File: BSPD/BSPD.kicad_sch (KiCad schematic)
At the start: 28 parts, among them J1 350826-1, J2 440054-2, Q1 NMOS, Q2 NMOS, Q3 PMOS, U1 LM339DR, U2 R-78E5.0-0.5, U4 SN74LVC3G14DCUR, U5 NE555DR, U6 SN74LVC1G08DBVR, U7 SN74AC32DR

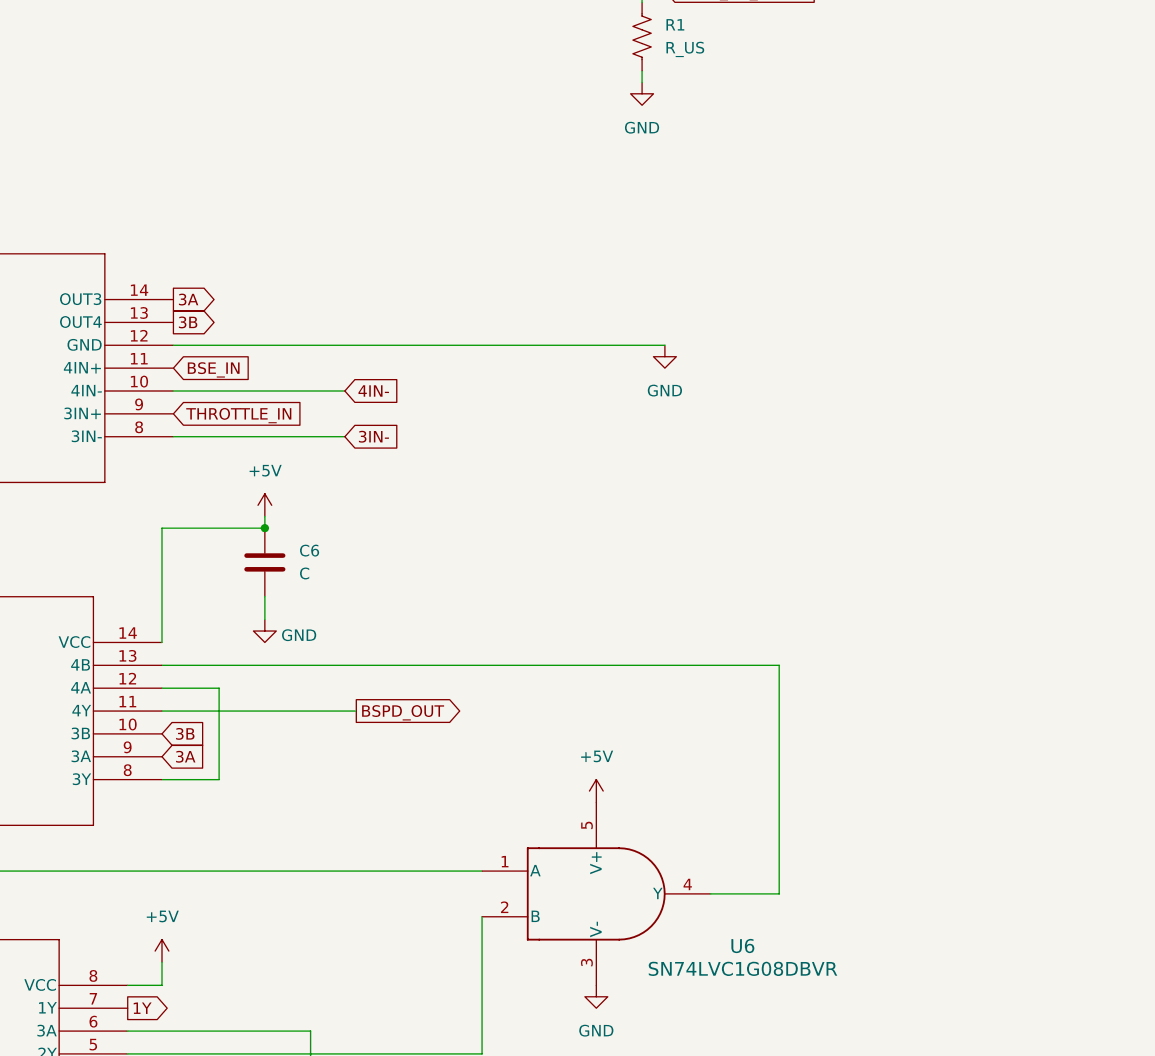
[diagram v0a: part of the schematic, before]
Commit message: Fixed one logical error. Added LT Spice simulation. Pullup Caps, resistor values, schematic layout and cleanup needed.
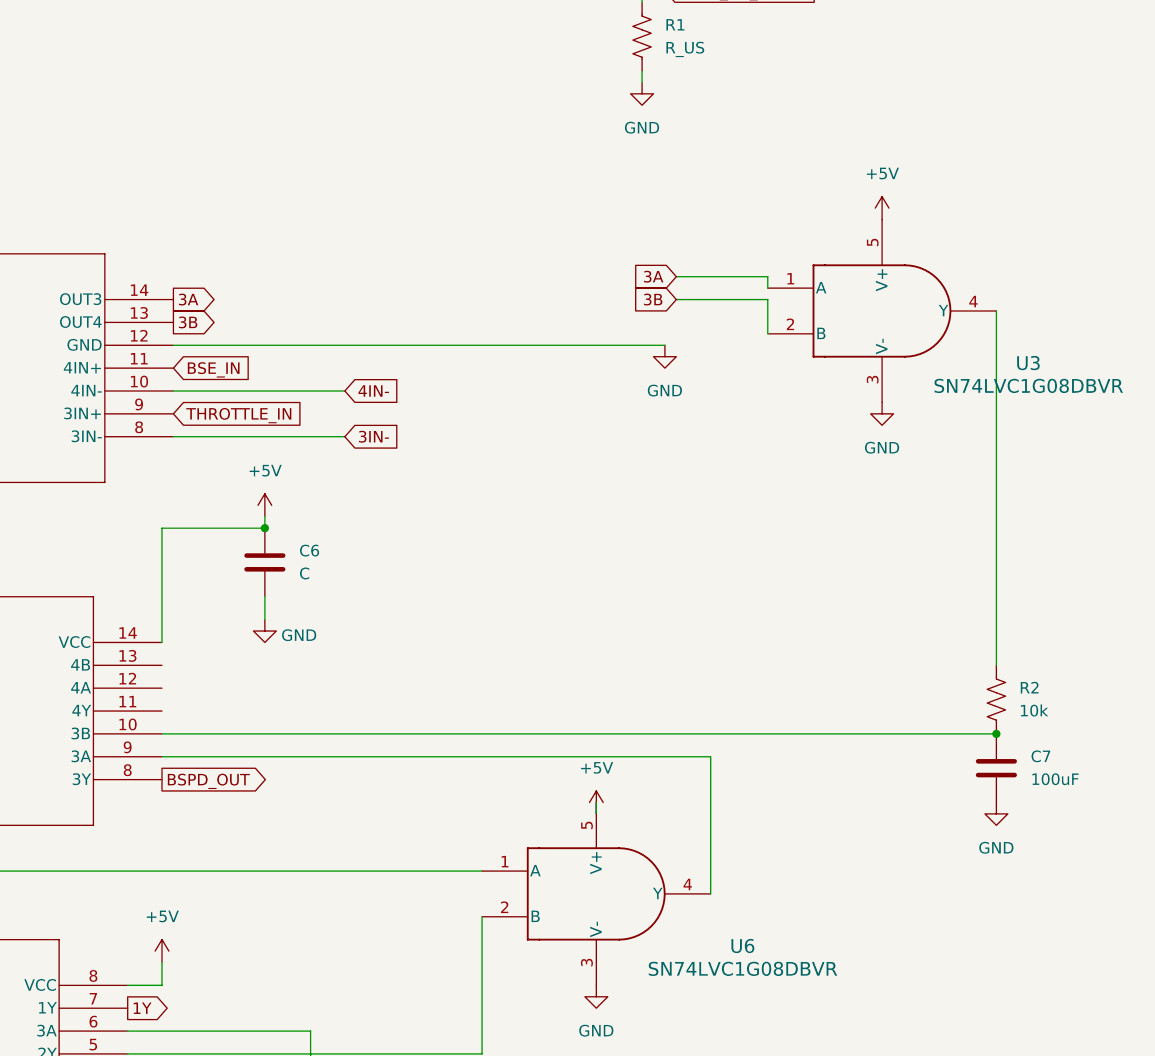
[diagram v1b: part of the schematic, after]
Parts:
- added C7: 100uF, symbol Device:C
- added R2: 10k, symbol Device:R_US
- added U3: SN74LVC1G08DBVR, SN74LVC1G08DBVR:DBV0005A_N, symbol SN74LVC1G08DBVR:SN74LVC1G08DBVR
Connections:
- net 3A: now also U3.1 (A); no longer U7.9 (3A)
- net 3B: now also U3.2 (B); no longer U7.10 (3B)
- net BSPD_OUT: now also U7.8 (3Y); no longer U7.11 (4Y)
- net GND: now also C7.2, U3.3 (V-)
- net at U7.12 (4A): no longer U7.8 (3Y)
- net at U7.13 (4B): no longer U6.4 (Y)
- new net: R2.1, U3.4 (Y)
- new net: C7.1, R2.2, U7.10 (3B)
- new net: U6.4 (Y), U7.9 (3A)

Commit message: Comments on BSPD, TSSI
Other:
- note added: "-AT FAULT - OUTPUT 0V"
- note added: "DC-DC Converter ; 12V-5V ; 500mA"
- note removed: "DC-DC Converter ; 12V-5V"
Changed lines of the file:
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@@
+		)
+	)
+	(text_box "-PLACE VALUES FOR COMPONENETS\n-USE SIMULATION AND VERIFY\n"
+		(exclude_from_sim no)
+		(at 33.02 193.675 0)
+		(size 89.535 13.97)
+		(stroke
+			(width 0)
+			(type default)
+		)
+		(fill
+			(type none)
+		)
+		(effects
+			(font
+				(size 1.27 1.27)
+			)
+			(justify left top)
 		)
 	)
@@
 		(exclude_from_sim no)
 		(at 75.692 176.784 0)
+		(effects
+			(font
+				(size 1.27 1.27)
+			)
+		)
+	)
+	(text "-AT FAULT - OUTPUT 0V\n"
+		(exclude_from_sim no)
+		(at 336.296 62.738 0)
 		(effects
 			(font
@@
 		)
 	)
-	(text "DC-DC Converter ; 12V-5V\n"
+	(text "DC-DC Converter ; 12V-5V ; 500mA\n"
 		(exclude_from_sim no)
-		(at 181.864 46.228 0)
+		(at 186.69 46.736 0)
 		(effects
 			(font

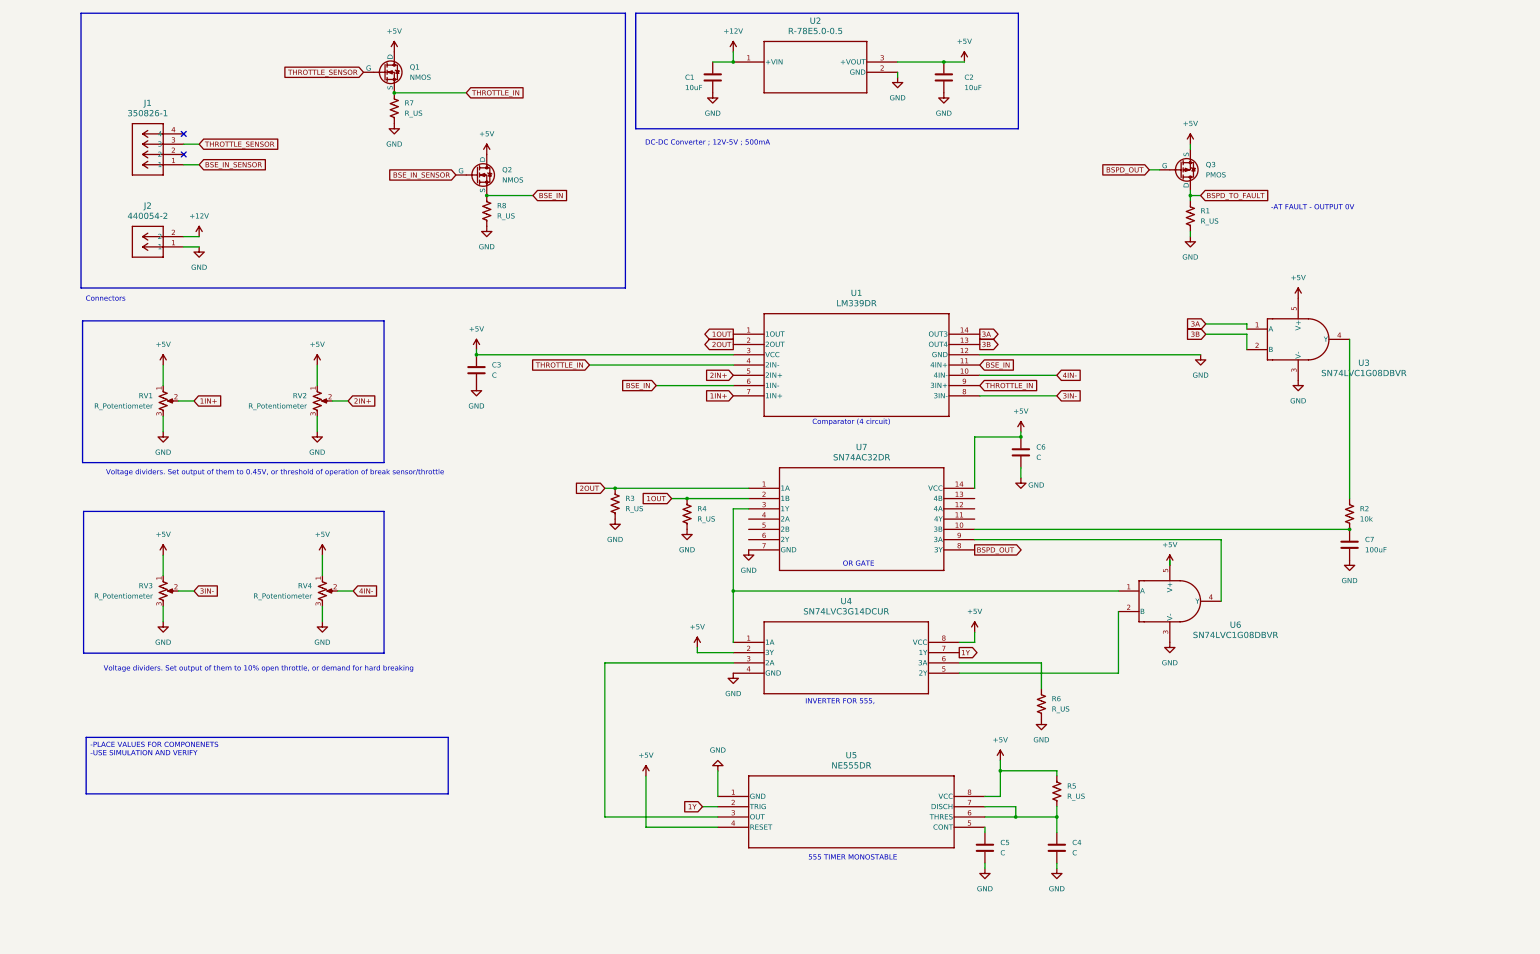
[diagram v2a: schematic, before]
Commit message: Added theory of operation to BSPD
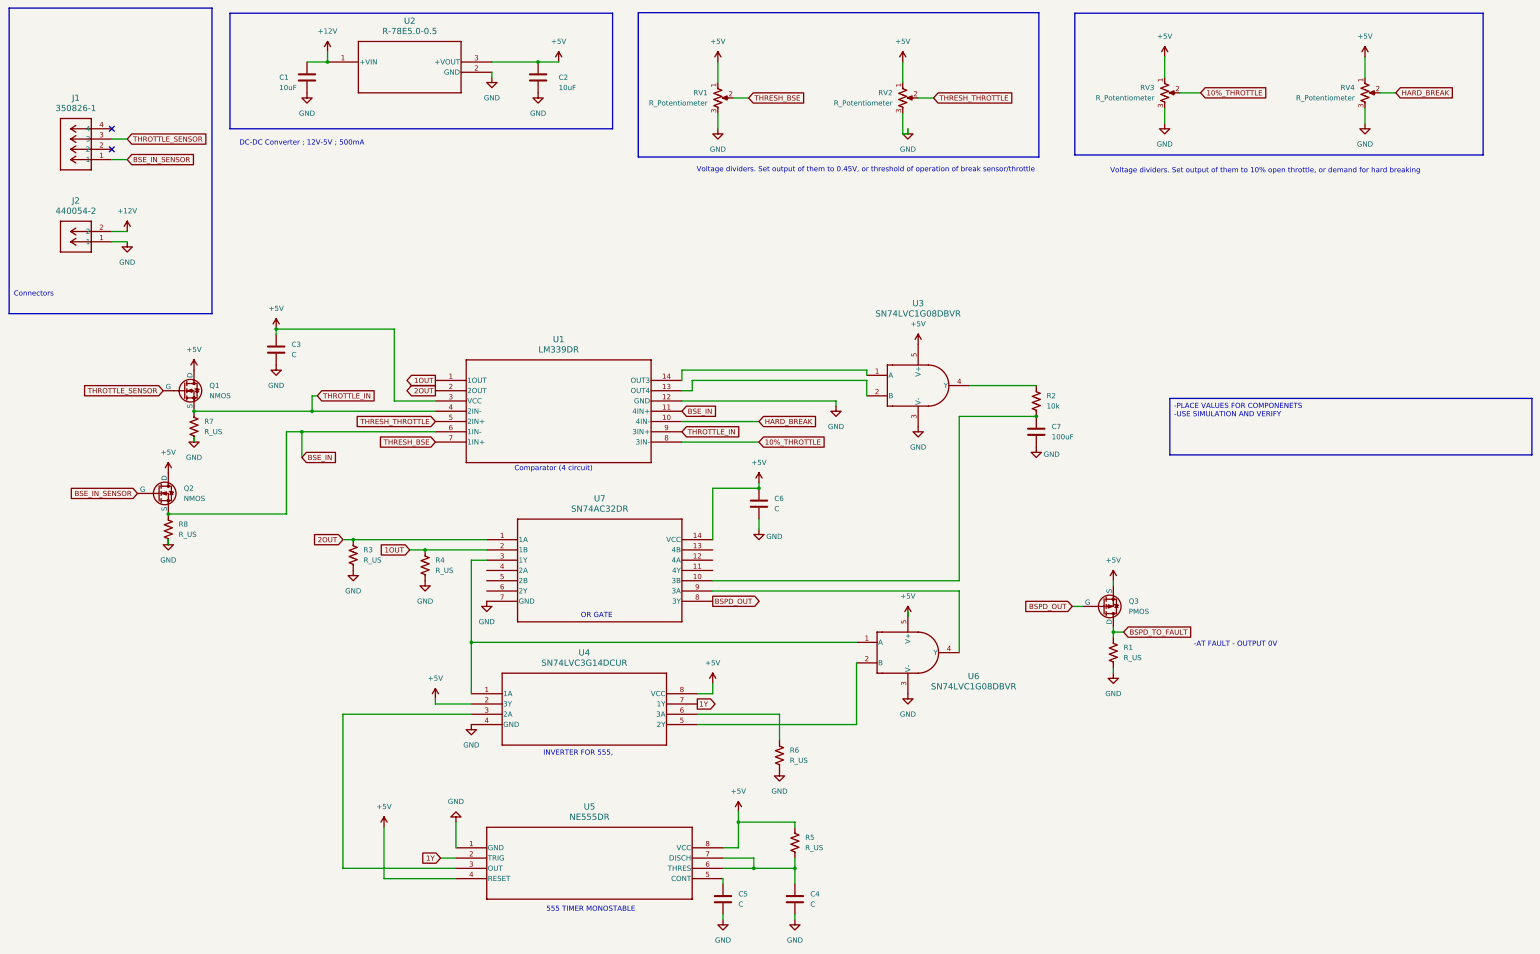
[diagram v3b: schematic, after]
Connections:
- net 1IN+ renamed THRESH_BSE
- net 2IN+ renamed THRESH_THROTTLE
- net 3A: no longer names the net of U1.14 (OUT3), U3.1 (A)
- net 3B: no longer names the net of U1.13 (OUT4), U3.2 (B)
- net 3IN- renamed 10%_THROTTLE
- net 4IN- renamed HARD_BREAK
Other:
- moved on the sheet: C1, C2, C3, C4, C5, C6, C7, J1, J2, Q1, Q2, Q3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

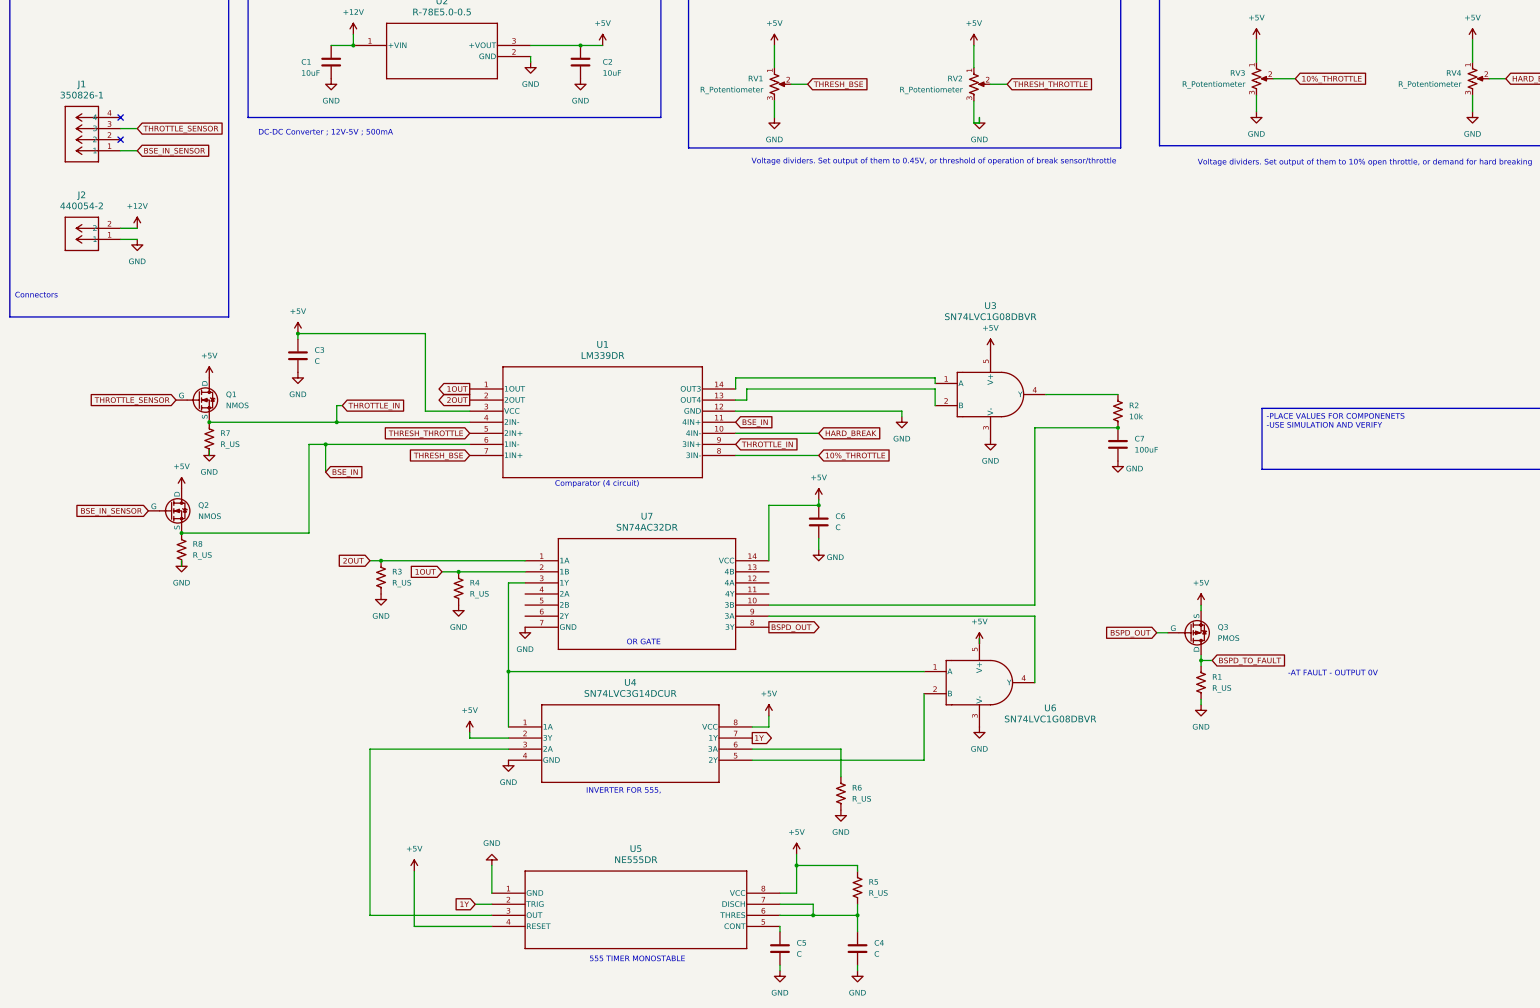
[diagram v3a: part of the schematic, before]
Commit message: Added footprints,implemented changes from meeting, starting layout
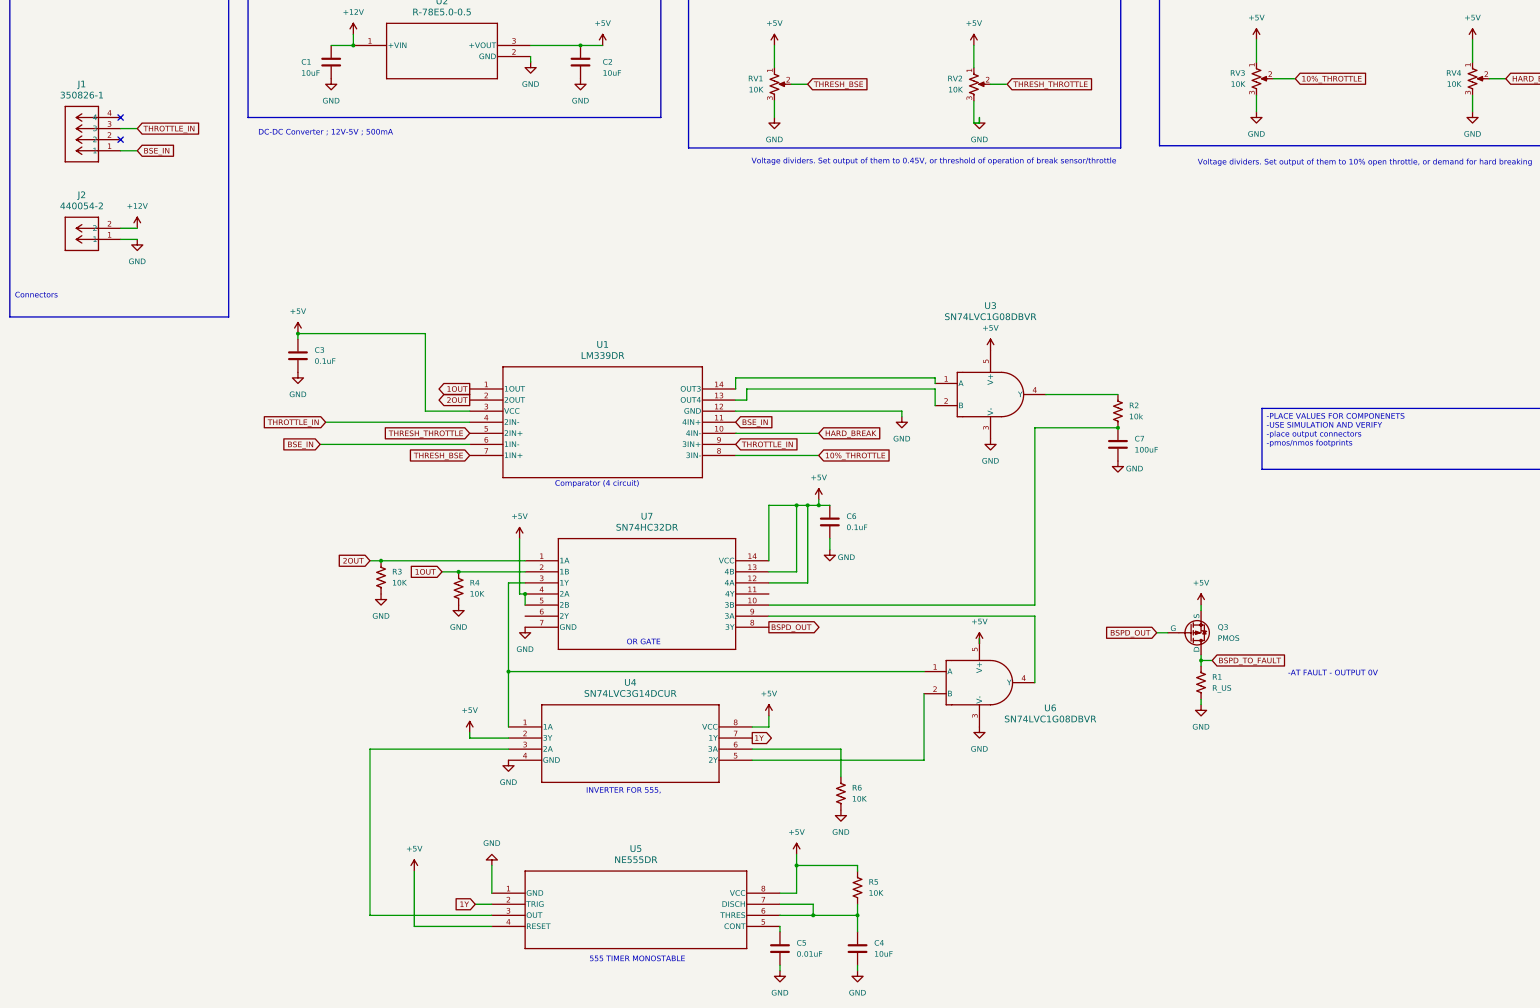
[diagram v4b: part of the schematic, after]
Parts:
- removed Q1, Q2: NMOS, symbol Simulation_SPICE:NMOS
- removed R7, R8: R_US, symbol Device:R_US
- C1, C2: footprint (none) -> Capacitor_SMD:C_0805_2012Metric
- C3, C6: value C -> 0.1uF; footprint (none) -> Capacitor_SMD:C_0805_2012Metric
- C4: value C -> 10uF; footprint (none) -> Capacitor_SMD:C_0805_2012Metric
- C5: value C -> 0.01uF; footprint (none) -> Capacitor_SMD:C_0805_2012Metric
- C7: footprint (none) -> Capacitor_SMD:C_1206_3216Metric
- R1: footprint (none) -> Resistor_SMD:R_0402_1005Metric
- R2: footprint (none) -> Resistor_SMD:R_0402_1005Metric_Pad0.72x0.64mm_HandSolder
- R3, R4, R5, R6: value R_US -> 10K; footprint (none) -> Resistor_SMD:R_0402_1005Metric_Pad0.72x0.64mm_HandSolder
- RV1, RV2, RV3, RV4: value R_Potentiometer -> 10K; footprint (none) -> PVG3A103C01R00:RES_C01R00
- U7: value SN74AC32DR -> SN74HC32DR; footprint D14 -> SN74AC32DR:D14
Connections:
- net BSE_IN_SENSOR is gone; now on net BSE_IN: J1.1
- net THROTTLE_SENSOR is gone; now on net THROTTLE_IN: J1.3
- net at C6.1, U7.14 (VCC): now also U7.12 (4A), U7.13 (4B)
- net at U7.4 (2A): now also U7.5 (2B)
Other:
- moved on the sheet: C6
